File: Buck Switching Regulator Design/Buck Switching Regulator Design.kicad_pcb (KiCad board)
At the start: 2 copper layers, 12 parts, among them U1 MP2322GQH-P

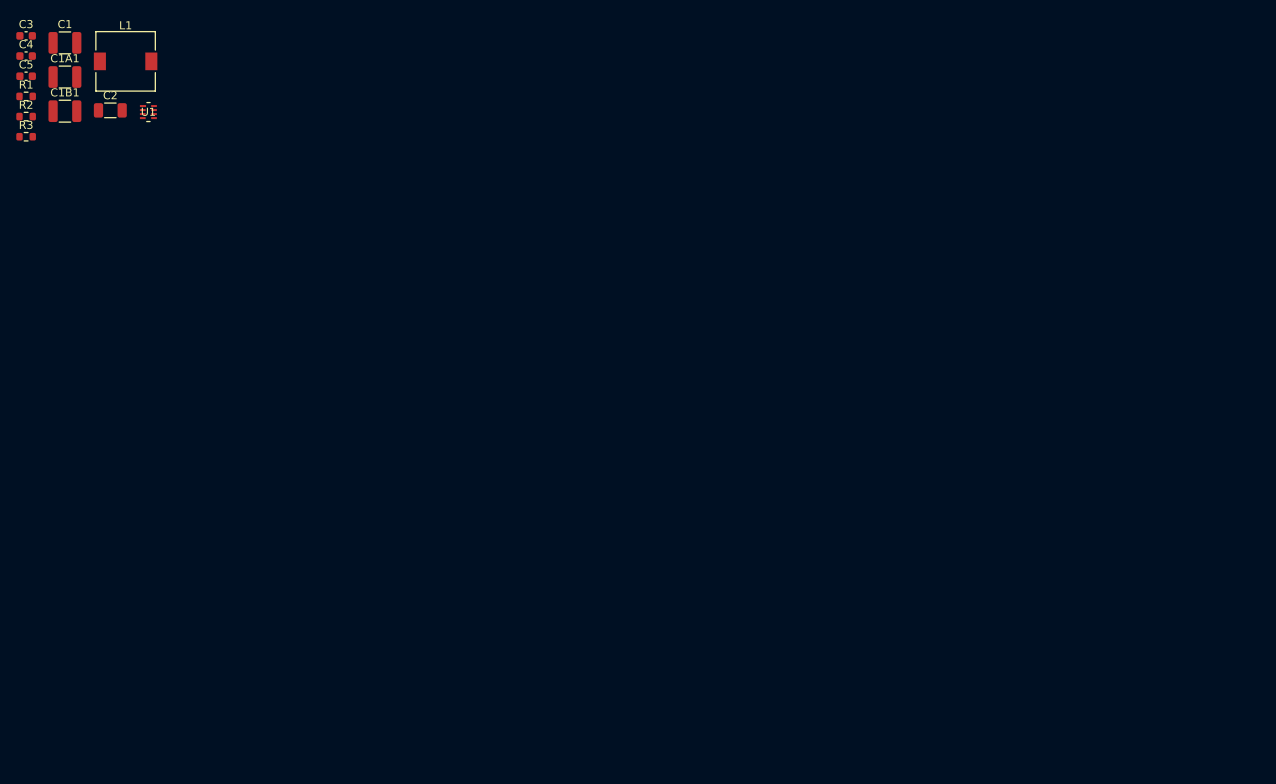
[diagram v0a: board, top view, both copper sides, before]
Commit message: PCB Layout: Components Placed
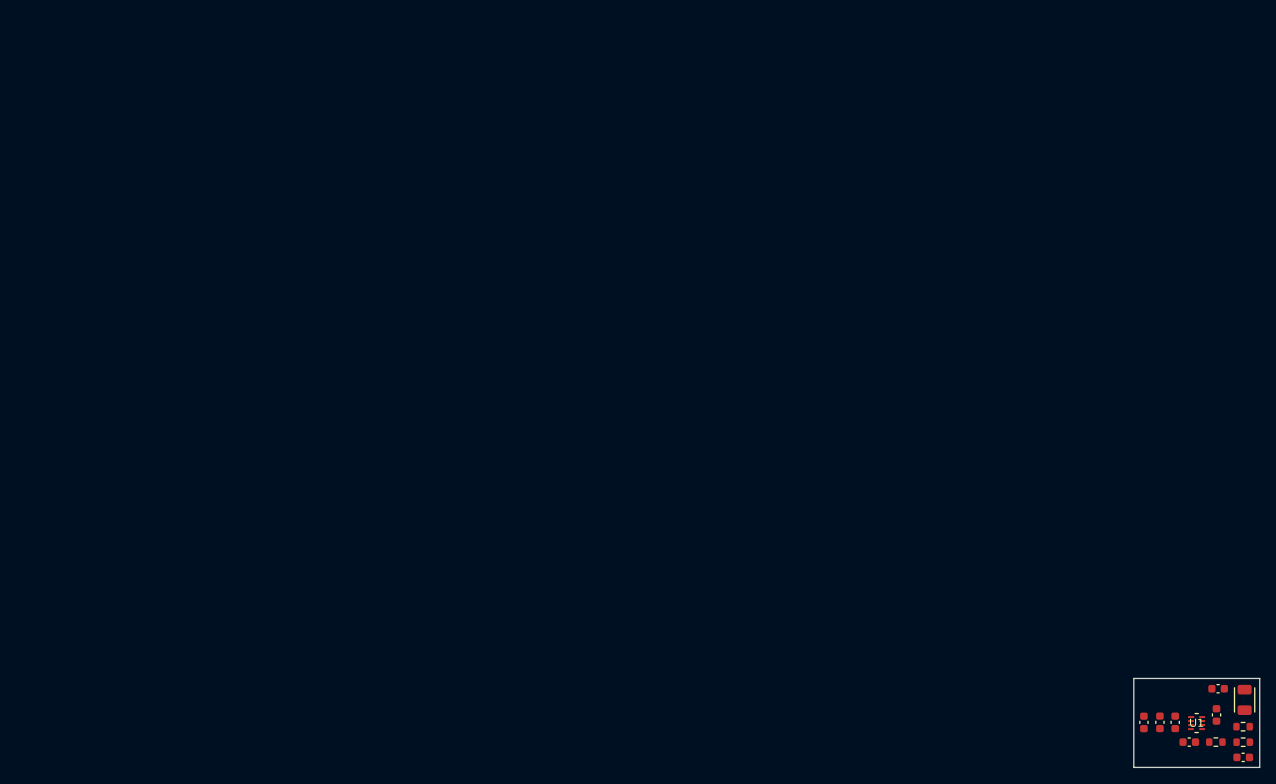
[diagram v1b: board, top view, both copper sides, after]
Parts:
- C1, C1A1, C1B1: footprint Capacitor_SMD:C_1210_3225Metric -> Capacitor_SMD:C_0603_1608Metric
- C2: footprint Capacitor_SMD:C_1206_3216Metric -> Capacitor_SMD:C_0603_1608Metric
- L1: footprint Inductor_SMD:L_7.3x7.3_H3.5 -> Inductor_SMD:L_Walsin_WLFM252009x
- moved C5 173.6 mm to (177.2, 114.7)
- moved R1 171.4 mm to (177.2, 112.8)
- moved C3 170.5 mm to (173.9, 109.4), turned to 90 degrees
- moved R3 168.3 mm to (177.2, 110.8)
- moved C4 168.0 mm to (170.5, 112.8)
- moved R2 167.3 mm to (173.8, 112.8)
- moved L1 160.3 mm to (177.4, 107.5), turned to 90 degrees
- moved C1 158.7 mm to (164.8, 110.3), turned to 90 degrees
- moved C1A1 158.2 mm to (166.8, 110.3), turned to 90 degrees
- moved C1B1 157.7 mm to (168.7, 110.3), turned to 90 degrees
- moved C2 155.5 mm to (174.1, 106.1)
- moved U1 151.0 mm to (171.4, 110.4)
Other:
- board outline added: 15.7 x 11.1 mm
